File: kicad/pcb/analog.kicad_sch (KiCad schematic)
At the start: 23 parts, among them U2 74HC4051, U5 OPA354

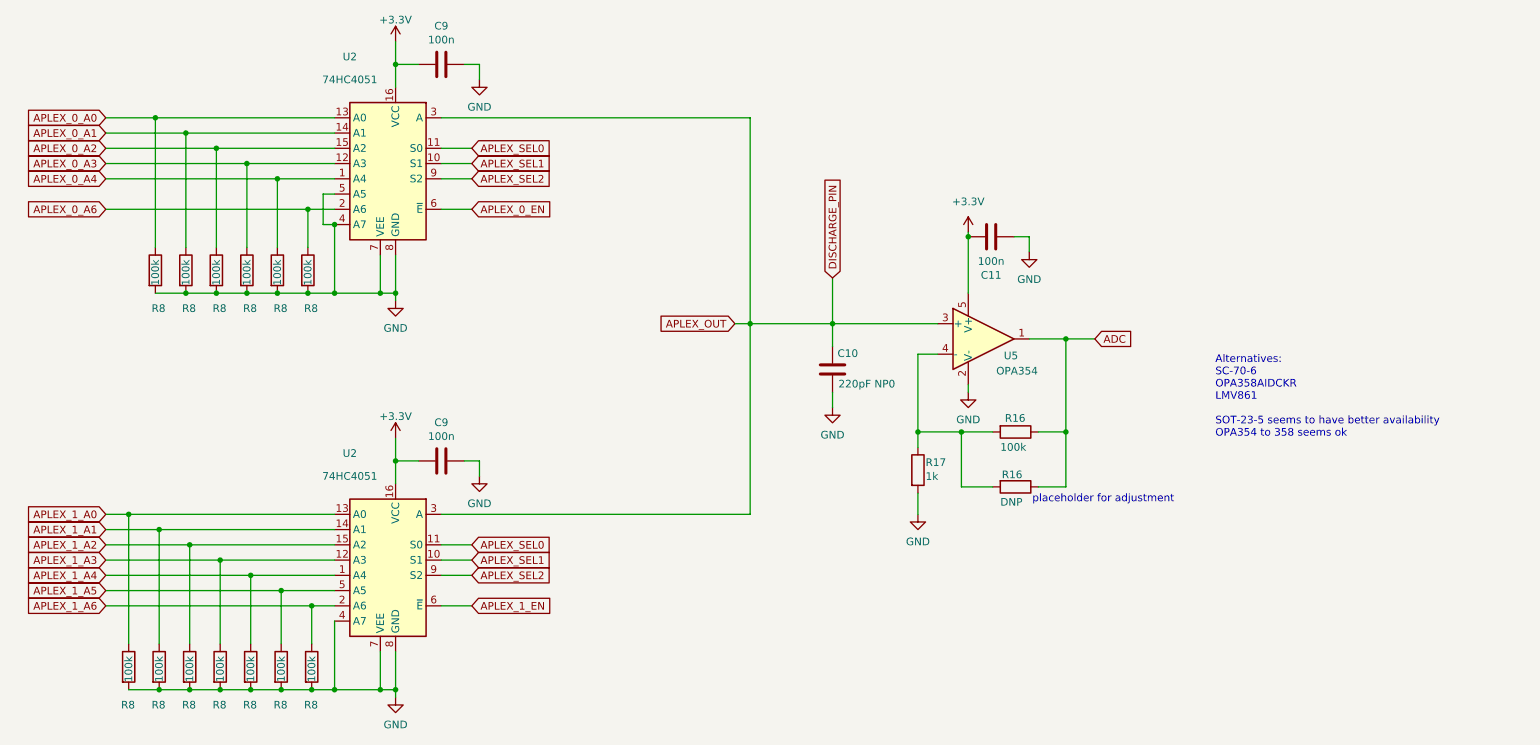
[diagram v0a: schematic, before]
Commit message: should be ok for proto order
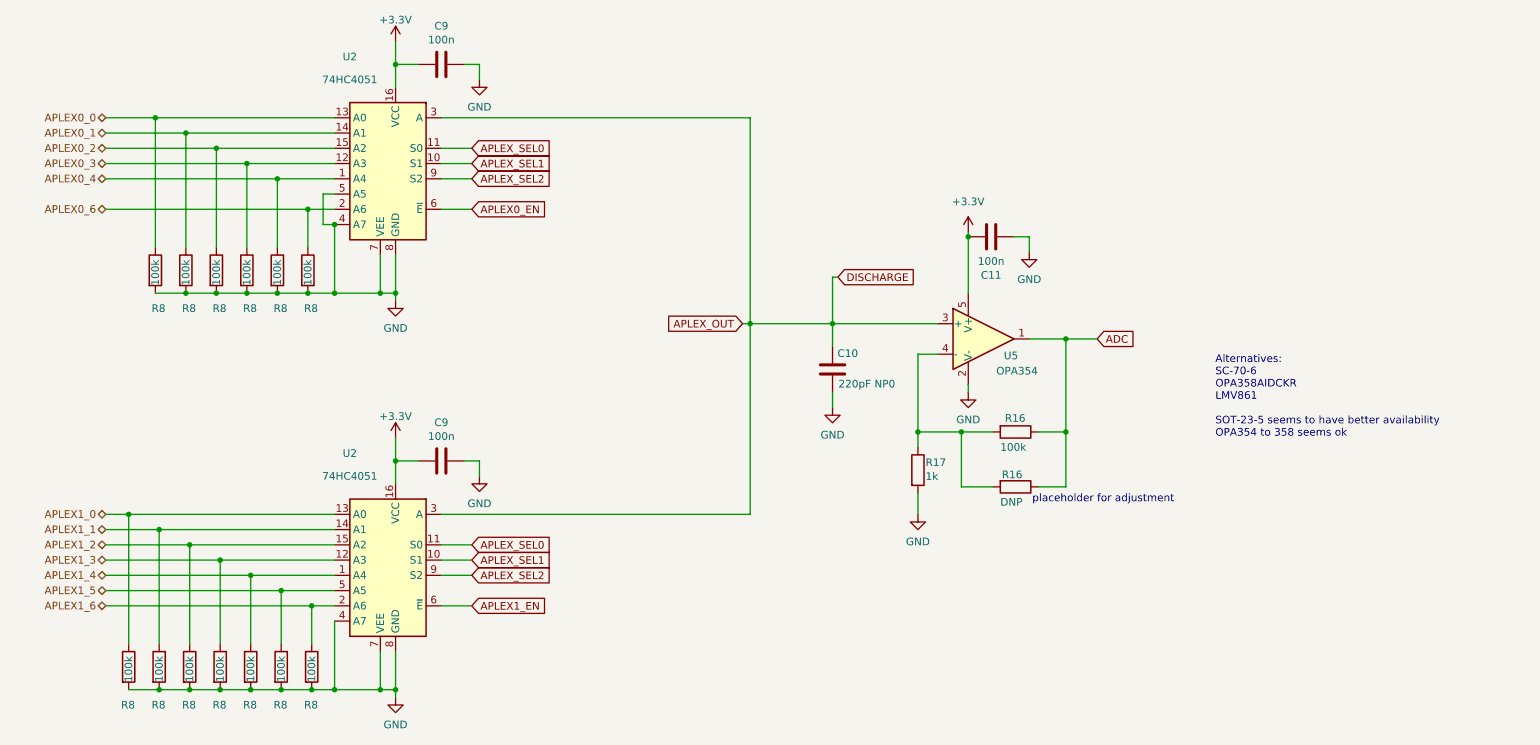
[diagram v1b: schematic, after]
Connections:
- net APLEX_0_A0 renamed APLEX0_0
- net APLEX_0_A1 renamed APLEX0_1
- net APLEX_0_A2 renamed APLEX0_2
- net APLEX_0_A3 renamed APLEX0_3
- net APLEX_0_A4 renamed APLEX0_4
- net APLEX_0_A6 renamed APLEX0_6
- net APLEX_0_EN renamed APLEX0_EN
- net APLEX_1_A0 renamed APLEX1_0
- net APLEX_1_A1 renamed APLEX1_1
- net APLEX_1_A2 renamed APLEX1_2
- net APLEX_1_A3 renamed APLEX1_3
- net APLEX_1_A4 renamed APLEX1_4
- net APLEX_1_A5 renamed APLEX1_5
- net APLEX_1_A6 renamed APLEX1_6
- net APLEX_1_EN renamed APLEX1_EN
